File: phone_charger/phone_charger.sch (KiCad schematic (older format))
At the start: 19 parts, among them J1 Conn_01x02, J2 SS-52100-001, U1 ADP2302

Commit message: Update DKPN and MPN fields
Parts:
- C1: Digi-Key_PN (none) -> 490-5525-1-ND; MPN (none) -> GRM319R61E106KA12D
- C2: MPN (none) -> ECJ-1V1C104K
- C3, C4: Digi-Key_PN (none) -> 490-10747-1-ND; MPN (none) -> GRM21BR61C226ME44L
- D1: Digi-Key_PN (none) -> 732-11403-ND; MPN (none) -> 151034RS03000
- D2: Digi-Key_PN (none) -> 641-1446-1-ND; MPN (none) -> CDBMT240-HF
- D3: Digi-Key_PN (none) -> 621-B330B-F; MPN (none) -> B330B-13-F
- F1: Digi-Key_PN (none) -> 507-1749-1-ND; MPN (none) -> 0ZCF0200AF2C
- J1: Digi-Key_PN (none) -> S1012EC-40-ND; MPN (none) -> PREC040SAAN-RC
- L1: Digi-Key_PN (none) -> 445-3561-1-ND; MPN (none) -> VLF10040T-6R8N4R5
- R2: Digi-Key_PN (none) -> RMCF0603FG100KCT-ND; MPN (none) -> RMCF0603FG100K
- R3: Digi-Key_PN (none) -> RMCF0805JT75K0CT-ND; MPN (none) -> RMCF0805JT75K0
- R4, R6: Digi-Key_PN (none) -> RHM46.4KCHCT-ND; MPN (none) -> MCR10ERTF4642
- R5: Digi-Key_PN (none) -> RHM43KCGCT-ND; MPN (none) -> MCR03ERTJ433
- U1: MPN (none) -> ADP2302ARDZ-R7
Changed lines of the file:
@@
 F 2 "phone_charger:L_TDK_VLF10040T-6R8N4R5" H 7250 1950 50  0001 C CNN
 F 3 "" H 7250 1950 50  0001 C CNN
+F 4 "445-3561-1-ND" H 0   0   50  0001 C CNN "Digi-Key_PN"
+F 5 "VLF10040T-6R8N4R5" H 0   0   50  0001 C CNN "MPN"
 	1    7250 1950
 	0    -1   -1   0
@@
 F 2 "Capacitors_SMD:C_0805_HandSoldering" H 8038 2000 50  0001 C CNN
 F 3 "" H 8000 2150 50  0001 C CNN
+F 4 "490-10747-1-ND" H 0   0   50  0001 C CNN "Digi-Key_PN"
+F 5 "GRM21BR61C226ME44L" H 0   0   50  0001 C CNN "MPN"
 	1    8000 2150
 	1    0    0    -1
@@
 F 2 "Diodes_SMD:D_SMB_Handsoldering" H 6900 2100 50  0001 C CNN
 F 3 "" H 6900 2100 50  0001 C CNN
+F 4 "621-B330B-F" H 0   0   50  0001 C CNN "Digi-Key_PN"
+F 5 "B330B-13-F" H 0   0   50  0001 C CNN "MPN"
 	1    6900 2100
 	0    1    1    0
@@
 F 2 "Capacitors_SMD:C_0603_HandSoldering" H 6938 1600 50  0001 C CNN
 F 3 "" H 6900 1750 50  0001 C CNN
+F 4 "ECJ-1V1C104K" H 0   0   50  0001 C CNN "MPN"
 	1    6900 1750
 	1    0    0    -1
@@
 F 2 "Capacitors_SMD:C_1206_HandSoldering" H 4738 1600 50  0001 C CNN
 F 3 "" H 4700 1750 50  0001 C CNN
+F 4 "490-5525-1-ND" H 0   0   50  0001 C CNN "Digi-Key_PN"
+F 5 "GRM319R61E106KA12D" H 0   0   50  0001 C CNN "MPN"
 	1    4700 1750
 	1    0    0    -1
@@
 F 2 "Resistors_SMD:R_0603_HandSoldering" V 5280 2100 50  0001 C CNN
 F 3 "" H 5350 2100 50  0001 C CNN
+F 4 "RMCF0603FG100KCT-ND" H 0   0   50  0001 C CNN "Digi-Key_PN"
+F 5 "RMCF0603FG100K" H 0   0   50  0001 C CNN "MPN"
 	1    5350 2100
 	1    0    0    -1
@@
 F 2 "Resistors_SMD:R_0805_HandSoldering" V 5330 3950 50  0001 C CNN
 F 3 "~" H 5400 3950 50  0001 C CNN
+F 4 "RMCF0805JT75K0CT-ND" H 0   0   50  0001 C CNN "Digi-Key_PN"
+F 5 "RMCF0805JT75K0" H 0   0   50  0001 C CNN "MPN"
 	1    5400 3950
 	1    0    0    -1
@@
 F 2 "Resistors_SMD:R_0805_HandSoldering" V 5330 4450 50  0001 C CNN
 F 3 "~" H 5400 4450 50  0001 C CNN
+F 4 "RHM46.4KCHCT-ND" H 0   0   50  0001 C CNN "Digi-Key_PN"
+F 5 "MCR10ERTF4642" H 0   0   50  0001 C CNN "MPN"
 	1    5400 4450
 	1    0    0    -1
@@
 F 2 "Resistors_SMD:R_0603_HandSoldering" V 5330 5250 50  0001 C CNN
 F 3 "~" H 5400 5250 50  0001 C CNN
+F 4 "RHM43KCGCT-ND" H 0   0   50  0001 C CNN "Digi-Key_PN"
+F 5 "MCR03ERTJ433" H 0   0   50  0001 C CNN "MPN"
 	1    5400 5250
 	1    0    0    -1
@@
 F 2 "Resistors_SMD:R_0805_HandSoldering" V 5330 5750 50  0001 C CNN
 F 3 "~" H 5400 5750 50  0001 C CNN
+F 4 "RHM46.4KCHCT-ND" H 0   0   50  0001 C CNN "Digi-Key_PN"
+F 5 "MCR10ERTF4642" H 0   0   50  0001 C CNN "MPN"
 	1    5400 5750
 	1    0    0    -1
@@
 F 1 "Polyfuse" V 2716 1600 50  0000 C CNN
 F 2 "Fuse_Holders_and_Fuses:Fuse_SMD2920" H 2900 1400 50  0001 L CNN
-F 3 "~" H 2850 1600 50  0001 C CNN
+F 3 "https://belfuse.com/resources/CircuitProtection/datasheets/0ZCF%20Nov2016.pdf" H 2850 1600 50  0001 C CNN
+F 4 "507-1749-1-ND" V 2850 1600 50  0001 C CNN "Digi-Key_PN"
+F 5 "0ZCF0200AF2C" V 2850 1600 50  0001 C CNN "MPN"
 	1    2850 1600
 	0    1    1    0
@@
 F 2 "Pin_Headers:Pin_Header_Straight_1x02_Pitch2.54mm" H 2200 1600 50  0001 C CNN
 F 3 "~" H 2200 1600 50  0001 C CNN
+F 4 "S1012EC-40-ND" H 0   0   50  0001 C CNN "Digi-Key_PN"
+F 5 "PREC040SAAN-RC" H 0   0   50  0001 C CNN "MPN"
 	1    2200 1600
 	-1   0    0    -1
@@
 F 3 "http://www.analog.com/media/en/technical-documentation/data-sheets/ADP2302_2303.pdf" H 6100 1800 60  0000 C CNN
 F 4 "584-ADP2302ARDZ-R7" H 6100 1950 50  0001 C CNN "Digi-Key_PN"
+F 5 "ADP2302ARDZ-R7" H 0   0   50  0001 C CNN "MPN"
 	1    6100 1950
 	1    0    0    -1
@@
 F 2 "Capacitors_SMD:C_0805_HandSoldering" H 7588 2000 50  0001 C CNN
 F 3 "" H 7550 2150 50  0001 C CNN
+F 4 "490-10747-1-ND" H 0   0   50  0001 C CNN "Digi-Key_PN"
+F 5 "GRM21BR61C226ME44L" H 0   0   50  0001 C CNN "MPN"
 	1    7550 2150
 	1    0    0    -1
@@
 F 2 "phone_charger:D_SOD-123" H 3550 1600 50  0001 C CNN
 F 3 "~" H 3550 1600 50  0001 C CNN
+F 4 "641-1446-1-ND" H 0   0   50  0001 C CNN "Digi-Key_PN"
+F 5 "CDBMT240-HF" H 0   0   50  0001 C CNN "MPN"
 	1    3550 1600
 	-1   0    0    1
@@
 F 2 "LEDs:LED_D3.0mm" H 3000 5000 50  0001 C CNN
 F 3 "~" H 3000 5000 50  0001 C CNN
+F 4 "732-11403-ND" H 0   0   50  0001 C CNN "Digi-Key_PN"
+F 5 "151034RS03000" H 0   0   50  0001 C CNN "MPN"
 	1    3000 5000
 	0    -1   -1   0

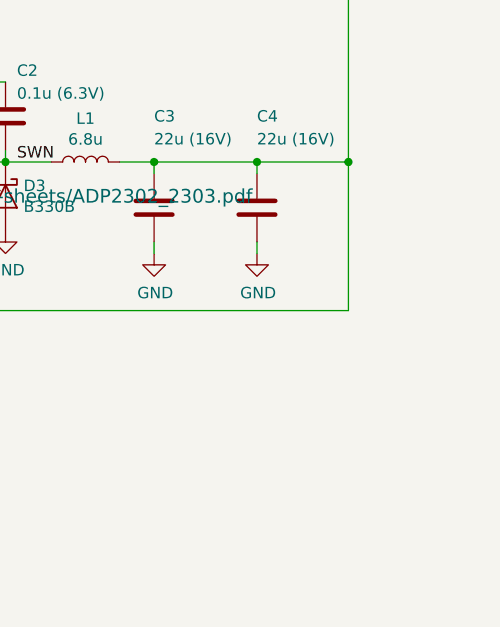
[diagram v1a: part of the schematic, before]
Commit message: Added fb resistors to phone charger
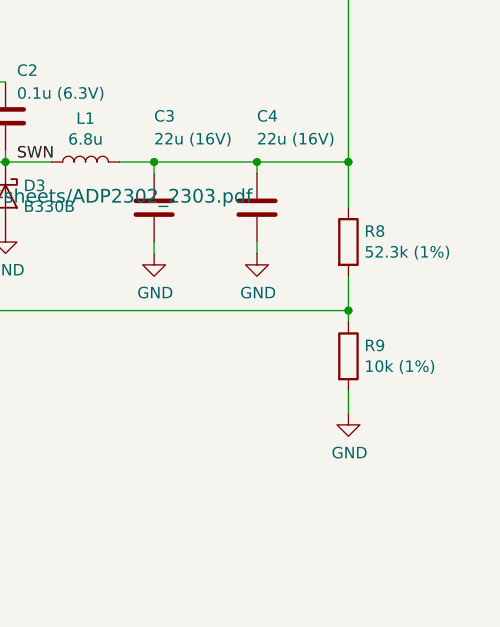
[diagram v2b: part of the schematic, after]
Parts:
- added R8: 52.3k (1%), Resistors_SMD:R_0603_HandSoldering, symbol Device:R
- added R9: 10k (1%), Resistors_SMD:R_0805_HandSoldering, symbol Device:R
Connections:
- net EPAD: now also R9.2
- net VBUS: now also R8.1; no longer U1.5 (FB)
- new net: R8.2, R9.1, U1.5 (FB)
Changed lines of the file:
@@
 Wire Wire Line
 	8000 1950 8400 1950
-Wire Wire Line
-	8400 2600 8400 1950
-Wire Wire Line
-	6750 2600 8400 2600
-Connection ~ 8400 1950
 $Comp
 L Device:D_Schottky D2
@@
 Text Label 6950 1950 0    50   ~ 0
 SWN
+$Comp
+L Device:R R8
+U 1 1 5BA427B1
+P 8400 2300
+F 0 "R8" H 8470 2346 50  0000 L CNN
+F 1 "52.3k (1%)" H 8470 2255 50  0000 L CNN
+F 2 "Resistors_SMD:R_0603_HandSoldering" V 8330 2300 50  0001 C CNN
+F 3 "~" H 8400 2300 50  0001 C CNN
+	1    8400 2300
+	1    0    0    -1
+$EndComp
+$Comp
+L Device:R R9
+U 1 1 5BA42AA2
+P 8400 2800
+F 0 "R9" H 8470 2846 50  0000 L CNN
+F 1 "10k (1%)" H 8470 2755 50  0000 L CNN
+F 2 "Resistors_SMD:R_0805_HandSoldering" V 8330 2800 50  0001 C CNN
+F 3 "~" H 8400 2800 50  0001 C CNN
+	1    8400 2800
+	1    0    0    -1
+$EndComp
+Wire Wire Line
+	6750 2600 8400 2600
+Wire Wire Line
+	8400 2600 8400 2450
+Wire Wire Line
+	8400 2150 8400 1950
+Connection ~ 8400 1950
+Wire Wire Line
+	8400 2600 8400 2650
+Connection ~ 8400 2600
+$Comp
+L power:GND #PWR0101
+U 1 1 5BA44B42
+P 8400 3050
+F 0 "#PWR0101" H 8400 2800 50  0001 C CNN
+F 1 "GND" H 8405 2877 50  0000 C CNN
+F 2 "" H 8400 3050 50  0001 C CNN
+F 3 "" H 8400 3050 50  0001 C CNN
+	1    8400 3050
+	1    0    0    -1
+$EndComp
+Wire Wire Line
+	8400 2950 8400 3050
 $EndSCHEMATC

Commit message: Updated LED hole size phone charger
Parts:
- D1: footprint LEDs:LED_D3.0mm -> phone_charger:LED_D3.0mm
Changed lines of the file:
@@
 F 0 "D1" V 3038 4883 50  0000 R CNN
 F 1 "LED" V 2947 4883 50  0000 R CNN
-F 2 "LEDs:LED_D3.0mm" H 3000 5000 50  0001 C CNN
+F 2 "phone_charger:LED_D3.0mm" H 3000 5000 50  0001 C CNN
 F 3 "~" H 3000 5000 50  0001 C CNN
 F 4 "732-11403-ND" H 0   0   50  0001 C CNN "Digi-Key_PN"

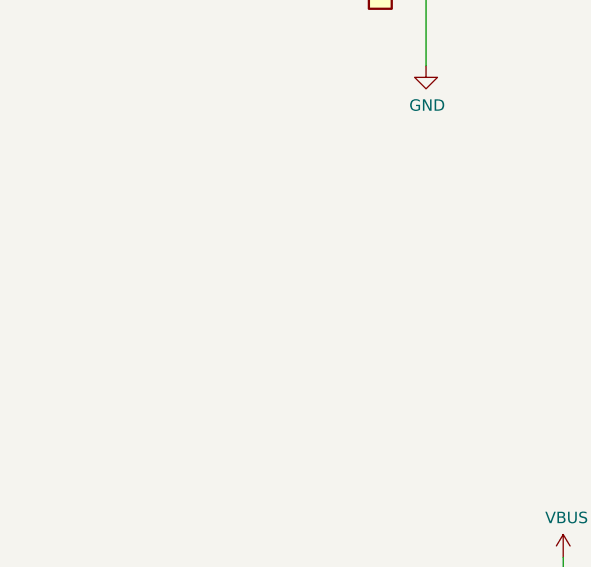
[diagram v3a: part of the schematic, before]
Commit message: updated schematic with silkscreen logos
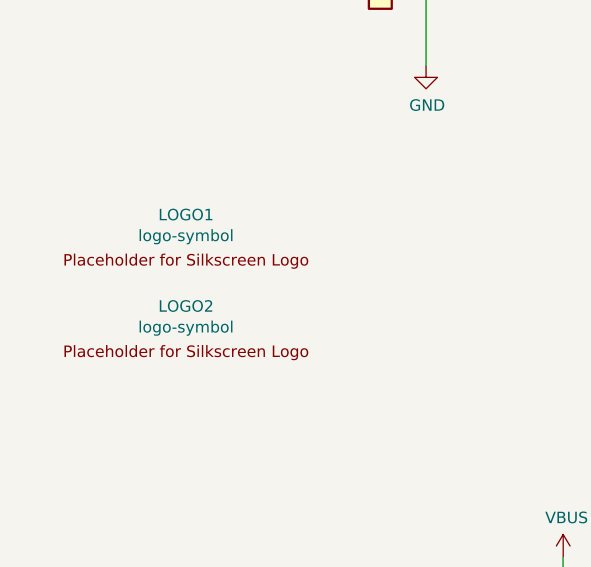
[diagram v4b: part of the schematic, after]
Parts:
- added LOGO1: logo-symbol, phone_charger:bac-logo, symbol phone_charger-rescue:logo-symbol
- added LOGO2: logo-symbol, phone_charger:ieee-logo-inv, symbol phone_charger-rescue:logo-symbol
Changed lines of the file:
@@
 Wire Wire Line
 	8400 2950 8400 3050
+$Comp
+L phone_charger-rescue:logo-symbol LOGO1
+U 1 1 5BA54FEB
+P 1350 2750
+F 0 "LOGO1" H 1350 2848 50  0000 C CNN
+F 1 "logo-symbol" H 1350 2757 50  0000 C CNN
+F 2 "phone_charger:bac-logo" H 1350 2750 50  0001 C CNN
+F 3 "" H 1350 2750 50  0001 C CNN
+	1    1350 2750
+	1    0    0    -1
+$EndComp
+$Comp
+L phone_charger-rescue:logo-symbol LOGO2
+U 1 1 5BA55205
+P 1350 3150
+F 0 "LOGO2" H 1350 3248 50  0000 C CNN
+F 1 "logo-symbol" H 1350 3157 50  0000 C CNN
+F 2 "phone_charger:ieee-logo-inv" H 1350 3150 50  0001 C CNN
+F 3 "" H 1350 3150 50  0001 C CNN
+	1    1350 3150
+	1    0    0    -1
+$EndComp
 $EndSCHEMATC

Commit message: Change diode package to 123H
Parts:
- D2: footprint phone_charger:D_SOD-123 -> Diode_SMD:D_SOD-123H
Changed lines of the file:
@@
 F 0 "D2" H 3550 1384 50  0000 C CNN
 F 1 "D_Schottky" H 3550 1475 50  0000 C CNN
-F 2 "phone_charger:D_SOD-123" H 3550 1600 50  0001 C CNN
+F 2 "Diode_SMD:D_SOD-123H" H 3550 1600 50  0001 C CNN
 F 3 "~" H 3550 1600 50  0001 C CNN
 F 4 "641-1446-1-ND" H 0   0   50  0001 C CNN "Digi-Key_PN"

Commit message: Final changes to diode footprint and final gerbers
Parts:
- D2: footprint Diode_SMD:D_SOD-123H -> phone_charger:D_SOD-123H
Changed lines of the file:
@@
 F 0 "D2" H 3550 1384 50  0000 C CNN
 F 1 "D_Schottky" H 3550 1475 50  0000 C CNN
-F 2 "Diode_SMD:D_SOD-123H" H 3550 1600 50  0001 C CNN
+F 2 "phone_charger:D_SOD-123H" H 3550 1600 50  0001 C CNN
 F 3 "~" H 3550 1600 50  0001 C CNN
 F 4 "641-1446-1-ND" H 0   0   50  0001 C CNN "Digi-Key_PN"

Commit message: Rev 2A
- Sync SMD footprints for R's and C's from 5.0.2
- Move diode symbol to silkscreen to indicate direction
- Add silkscreen box around inductor
- Indicate bottom of USB connector on silkscreen
- Fix silkscreen component designators
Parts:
- C1: footprint Capacitors_SMD:C_1206_HandSoldering -> Capacitor_SMD:C_1206_3216Metric_Pad1.42x1.75mm_HandSolder
- C2: footprint Capacitors_SMD:C_0603_HandSoldering -> Capacitor_SMD:C_0603_1608Metric_Pad1.05x0.95mm_HandSolder
- C3, C4: footprint Capacitors_SMD:C_0805_HandSoldering -> Capacitor_SMD:C_0805_2012Metric_Pad1.15x1.40mm_HandSolder
- D3: footprint Diodes_SMD:D_SMB_Handsoldering -> phone_charger:D_SMB_Handsoldering
- R2, R5, R7, R8: footprint Resistors_SMD:R_0603_HandSoldering -> Resistor_SMD:R_0603_1608Metric_Pad1.05x0.95mm_HandSolder
- R3, R4, R6, R9: footprint Resistors_SMD:R_0805_HandSoldering -> Resistor_SMD:R_0805_2012Metric_Pad1.15x1.40mm_HandSolder
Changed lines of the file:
@@
 encoding utf-8
 Sheet 1 1
-Title ""
-Date ""
-Rev ""
-Comp ""
-Comment1 ""
-Comment2 ""
+Title "Phone Charger"
+Date "2018-09-20"
+Rev "A"
+Comp "Hands-On PCB Engineering"
+Comment1 "Kevin Zheng"
+Comment2 "Olivia Hsu"
 Comment3 ""
 Comment4 ""
@@
 F 0 "C4" H 8000 2550 50  0000 L CNN
 F 1 "22u (16V)" H 8000 2450 50  0000 L CNN
-F 2 "Capacitors_SMD:C_0805_HandSoldering" H 8038 2000 50  0001 C CNN
+F 2 "Capacitor_SMD:C_0805_2012Metric_Pad1.15x1.40mm_HandSolder" H 8038 2000 50  0001 C CNN
 F 3 "" H 8000 2150 50  0001 C CNN
 F 4 "490-10747-1-ND" H 0   0   50  0001 C CNN "Digi-Key_PN"
@@
 F 0 "D3" V 6854 2179 50  0000 L CNN
 F 1 "B330B" V 6945 2179 50  0000 L CNN
-F 2 "Diodes_SMD:D_SMB_Handsoldering" H 6900 2100 50  0001 C CNN
+F 2 "phone_charger:D_SMB_Handsoldering" H 6900 2100 50  0001 C CNN
 F 3 "" H 6900 2100 50  0001 C CNN
 F 4 "621-B330B-F" H 0   0   50  0001 C CNN "Digi-Key_PN"
@@
 F 0 "C2" H 6950 1950 50  0000 L CNN
 F 1 "0.1u (6.3V)" H 6950 1850 50  0000 L CNN
-F 2 "Capacitors_SMD:C_0603_HandSoldering" H 6938 1600 50  0001 C CNN
+F 2 "Capacitor_SMD:C_0603_1608Metric_Pad1.05x0.95mm_HandSolder" H 6938 1600 50  0001 C CNN
 F 3 "" H 6900 1750 50  0001 C CNN
 F 4 "ECJ-1V1C104K" H 0   0   50  0001 C CNN "MPN"
@@
 F 0 "C1" H 4815 1796 50  0000 L CNN
 F 1 "10u (25V)" H 4815 1705 50  0000 L CNN
-F 2 "Capacitors_SMD:C_1206_HandSoldering" H 4738 1600 50  0001 C CNN
+F 2 "Capacitor_SMD:C_1206_3216Metric_Pad1.42x1.75mm_HandSolder" H 4738 1600 50  0001 C CNN
 F 3 "" H 4700 1750 50  0001 C CNN
 F 4 "490-5525-1-ND" H 0   0   50  0001 C CNN "Digi-Key_PN"
@@
 F 0 "R2" H 5420 2146 50  0000 L CNN
 F 1 "100k" H 5420 2055 50  0000 L CNN
-F 2 "Resistors_SMD:R_0603_HandSoldering" V 5280 2100 50  0001 C CNN
+F 2 "Resistor_SMD:R_0603_1608Metric_Pad1.05x0.95mm_HandSolder" V 5280 2100 50  0001 C CNN
 F 3 "" H 5350 2100 50  0001 C CNN
 F 4 "RMCF0603FG100KCT-ND" H 0   0   50  0001 C CNN "Digi-Key_PN"
@@
 F 0 "R3" H 5470 3996 50  0000 L CNN
 F 1 "75k" H 5470 3905 50  0000 L CNN
-F 2 "Resistors_SMD:R_0805_HandSoldering" V 5330 3950 50  0001 C CNN
+F 2 "Resistor_SMD:R_0805_2012Metric_Pad1.15x1.40mm_HandSolder" V 5330 3950 50  0001 C CNN
 F 3 "~" H 5400 3950 50  0001 C CNN
 F 4 "RMCF0805JT75K0CT-ND" H 0   0   50  0001 C CNN "Digi-Key_PN"
@@
 F 0 "R4" H 5470 4496 50  0000 L CNN
 F 1 "50k" H 5470 4405 50  0000 L CNN
-F 2 "Resistors_SMD:R_0805_HandSoldering" V 5330 4450 50  0001 C CNN
+F 2 "Resistor_SMD:R_0805_2012Metric_Pad1.15x1.40mm_HandSolder" V 5330 4450 50  0001 C CNN
 F 3 "~" H 5400 4450 50  0001 C CNN
 F 4 "RHM46.4KCHCT-ND" H 0   0   50  0001 C CNN "Digi-Key_PN"
@@
 F 0 "R5" H 5470 5296 50  0000 L CNN
 F 1 "43k" H 5470 5205 50  0000 L CNN
-F 2 "Resistors_SMD:R_0603_HandSoldering" V 5330 5250 50  0001 C CNN
+F 2 "Resistor_SMD:R_0603_1608Metric_Pad1.05x0.95mm_HandSolder" V 5330 5250 50  0001 C CNN
 F 3 "~" H 5400 5250 50  0001 C CNN
 F 4 "RHM43KCGCT-ND" H 0   0   50  0001 C CNN "Digi-Key_PN"
@@
 F 0 "R6" H 5470 5796 50  0000 L CNN
 F 1 "50k" H 5470 5705 50  0000 L CNN
-F 2 "Resistors_SMD:R_0805_HandSoldering" V 5330 5750 50  0001 C CNN
+F 2 "Resistor_SMD:R_0805_2012Metric_Pad1.15x1.40mm_HandSolder" V 5330 5750 50  0001 C CNN
 F 3 "~" H 5400 5750 50  0001 C CNN
 F 4 "RHM46.4KCHCT-ND" H 0   0   50  0001 C CNN "Digi-Key_PN"
@@
 F 0 "R7" H 5750 5050 50  0000 L CNN
 F 1 "0R (OPT)" H 5750 4950 50  0000 L CNN
-F 2 "Resistors_SMD:R_0603_HandSoldering" V 5630 4750 50  0001 C CNN
+F 2 "Resistor_SMD:R_0603_1608Metric_Pad1.05x0.95mm_HandSolder" V 5630 4750 50  0001 C CNN
 F 3 "~" H 5700 4750 50  0001 C CNN
 	1    5700 4750
@@
 F 0 "C3" H 7550 2550 50  0000 L CNN
 F 1 "22u (16V)" H 7550 2450 50  0000 L CNN
-F 2 "Capacitors_SMD:C_0805_HandSoldering" H 7588 2000 50  0001 C CNN
+F 2 "Capacitor_SMD:C_0805_2012Metric_Pad1.15x1.40mm_HandSolder" H 7588 2000 50  0001 C CNN
 F 3 "" H 7550 2150 50  0001 C CNN
 F 4 "490-10747-1-ND" H 0   0   50  0001 C CNN "Digi-Key_PN"
@@
 F 0 "R8" H 8470 2346 50  0000 L CNN
 F 1 "52.3k (1%)" H 8470 2255 50  0000 L CNN
-F 2 "Resistors_SMD:R_0603_HandSoldering" V 8330 2300 50  0001 C CNN
+F 2 "Resistor_SMD:R_0603_1608Metric_Pad1.05x0.95mm_HandSolder" V 8330 2300 50  0001 C CNN
 F 3 "~" H 8400 2300 50  0001 C CNN
 	1    8400 2300
@@
 F 0 "R9" H 8470 2846 50  0000 L CNN
 F 1 "10k (1%)" H 8470 2755 50  0000 L CNN
-F 2 "Resistors_SMD:R_0805_HandSoldering" V 8330 2800 50  0001 C CNN
+F 2 "Resistor_SMD:R_0805_2012Metric_Pad1.15x1.40mm_HandSolder" V 8330 2800 50  0001 C CNN
 F 3 "~" H 8400 2800 50  0001 C CNN
 	1    8400 2800
